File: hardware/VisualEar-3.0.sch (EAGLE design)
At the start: 8 parts

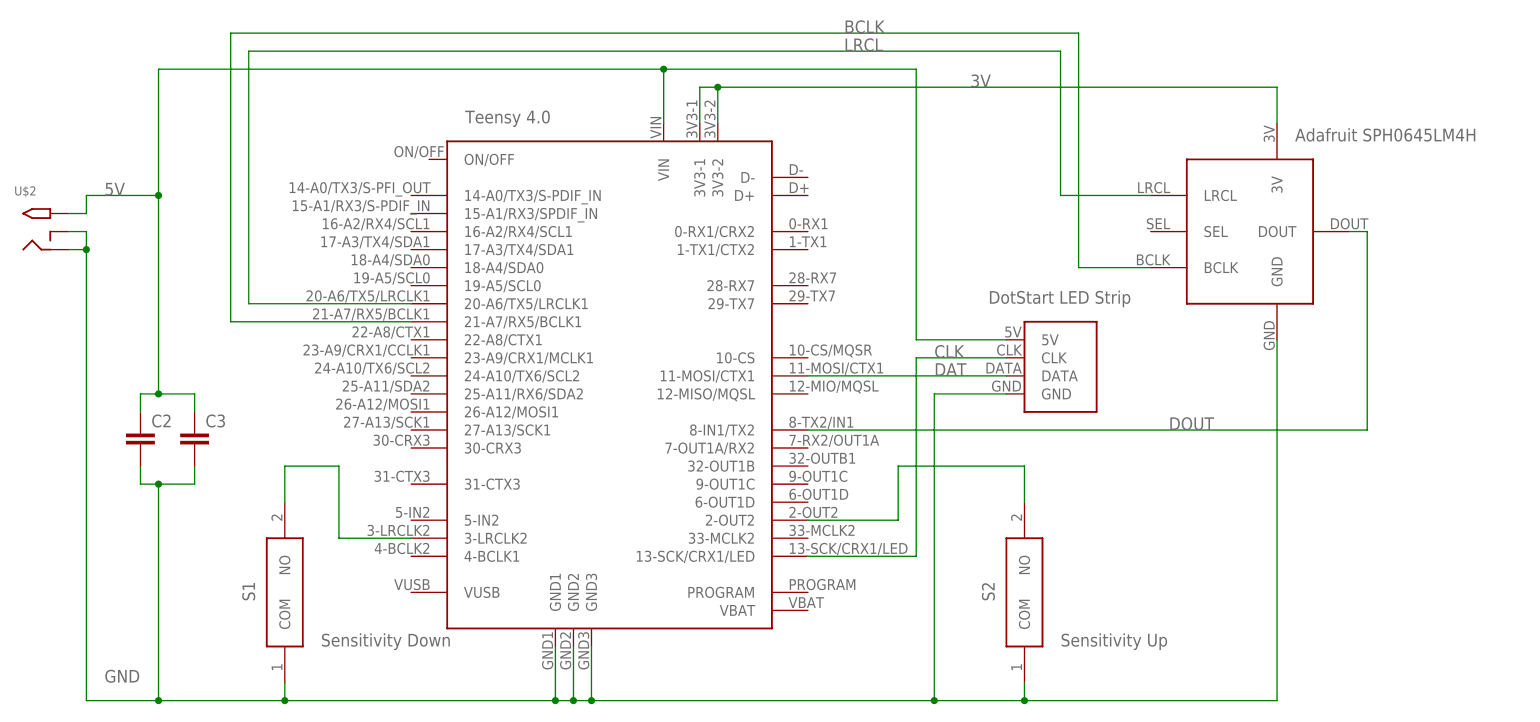
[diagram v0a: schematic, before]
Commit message: Updated to Single Button 3.0 PCB
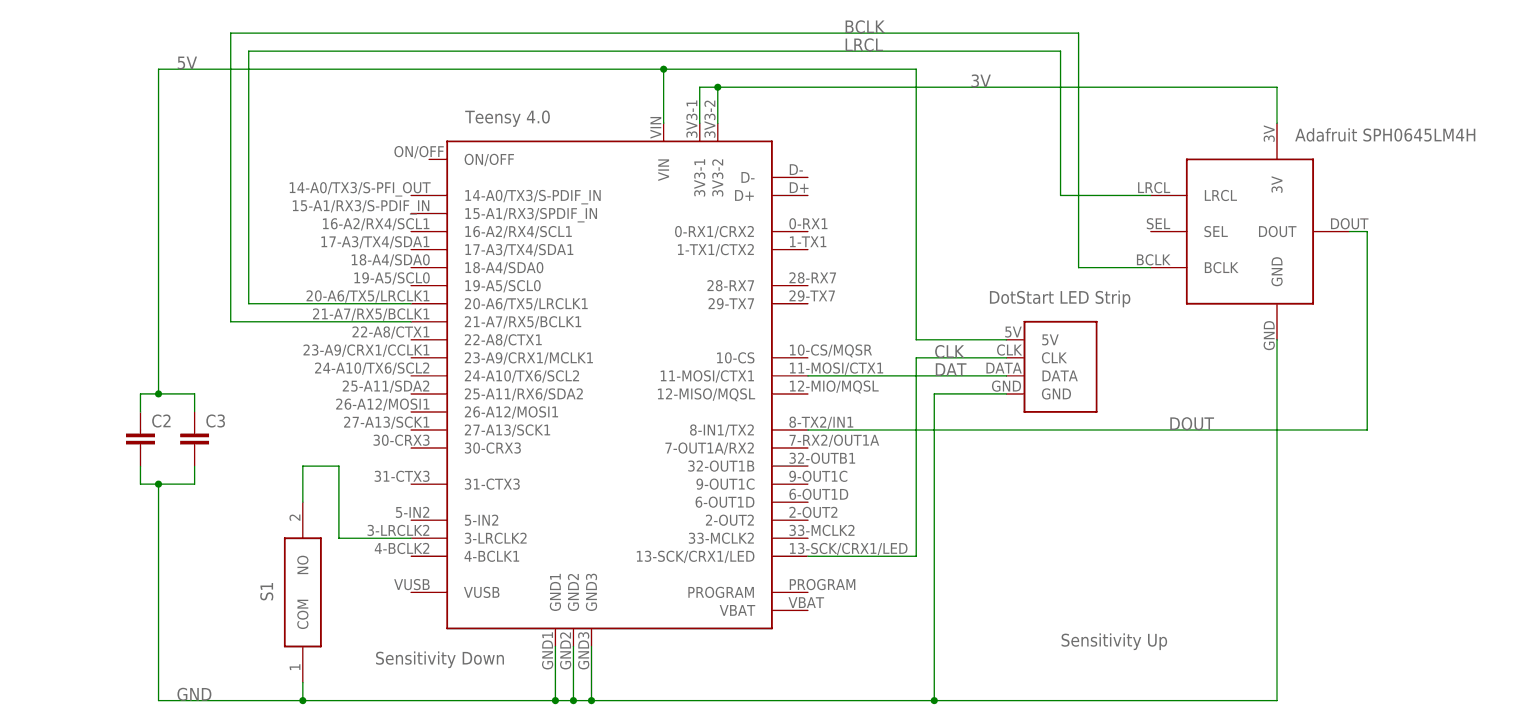
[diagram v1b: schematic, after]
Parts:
- removed S2: TACTILE-SWITCHTHRU-HOLE, philbot:TACTILE-SWITCHTHRU-HOLE
- removed U$2: 2.1MMJACKTHM, philbot:2.1MMJACKTHM
- C2, C3: device philbot:CAPPTH -> philbot:CAPPTH3
- U$1: value TEENSY40DIP -> TEENSY40DIPPLUS5; device teensy:TEENSY40DIP -> teensy:TEENSY40DIPPLUS5
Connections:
- removed net N$1: S2.NO, U$1.2-OUT2
- net 5V: no longer U$2.TIP
- net GND: no longer S2.COM, U$2.RING, U$2.RING_SW
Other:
- moved on the sheet: S1
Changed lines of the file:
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@@
 </classes>
 <parts>
-<part name="U$1" library="teensy" deviceset="TEENSY40" device="DIP" value="TEENSY40DIP"/>
-<part name="U$2" library="philbot" deviceset="2.1MMJACK" device="THM"/>
+<part name="U$1" library="teensy" deviceset="TEENSY40" device="DIPPLUS5" value="TEENSY40DIPPLUS5"/>
 <part name="U$3" library="philbot" deviceset="AF-I2S-MIC" device=""/>
 <part name="U$4" library="philbot" deviceset="LED-STRIP" device=""/>
-<part name="C2" library="philbot" deviceset="CAP" device="PTH"/>
-<part name="C3" library="philbot" deviceset="CAP" device="PTH"/>
+<part name="C2" library="philbot" deviceset="CAP" device="PTH3"/>
+<part name="C3" library="philbot" deviceset="CAP" device="PTH3"/>
 <part name="S1" library="philbot" deviceset="TACTILE-SWITCH" device="THRU-HOLE"/>
-<part name="S2" library="philbot" deviceset="TACTILE-SWITCH" device="THRU-HOLE"/>
 </parts>
 <sheets>
@@
 <text x="134.62" y="86.36" size="1.778" layer="95">Adafruit SPH0645LM4H</text>
 <text x="17.78" y="88.9" size="1.778" layer="95">Teensy 4.0</text>
-<text x="-2.54" y="15.24" size="1.778" layer="95">Sensitivity Down</text>
+<text x="5.08" y="12.7" size="1.778" layer="95">Sensitivity Down</text>
 <text x="101.6" y="15.24" size="1.778" layer="95">Sensitivity Up</text>
 </plain>
 <instances>
 <instance part="U$1" gate="G$1" x="38.1" y="55.88" smashed="yes"/>
-<instance part="U$2" gate="G$1" x="-43.18" y="73.66" smashed="yes">
-<attribute name="NAME" x="-45.72" y="78.74" size="1.27" layer="95"/>
-</instance>
 <instance part="U$3" gate="G$1" x="127" y="73.66" smashed="yes"/>
 <instance part="U$4" gate="G$1" x="99.06" y="53.34" smashed="yes"/>
@@
 <attribute name="VALUE" x="-18.796" y="41.021" size="1.778" layer="96"/>
 </instance>
-<instance part="S1" gate="G$1" x="-7.62" y="10.16" smashed="yes" rot="R90">
-<attribute name="NAME" x="-12.7" y="21.59" size="1.778" layer="95" rot="R90" align="center-left"/>
-</instance>
-<instance part="S2" gate="G$1" x="96.52" y="10.16" smashed="yes" rot="R90">
-<attribute name="NAME" x="91.44" y="21.59" size="1.778" layer="95" rot="R90" align="center-left"/>
+<instance part="S1" gate="G$1" x="-5.08" y="10.16" smashed="yes" rot="R90">
+<attribute name="NAME" x="-10.16" y="21.59" size="1.778" layer="95" rot="R90" align="center-left"/>
 </instance>
 </instances>
@@
 <net name="5V" class="0">
 <segment>
-<pinref part="U$2" gate="G$1" pin="TIP"/>
-<wire x1="-38.1" y1="76.2" x2="-35.56" y2="76.2" width="0.1524" layer="91"/>
-<wire x1="-35.56" y1="76.2" x2="-35.56" y2="78.74" width="0.1524" layer="91"/>
-<wire x1="-35.56" y1="78.74" x2="-25.4" y2="78.74" width="0.1524" layer="91"/>
 <pinref part="U$1" gate="G$1" pin="VIN"/>
 <wire x1="45.72" y1="88.9" x2="45.72" y2="96.52" width="0.1524" layer="91"/>
 <wire x1="45.72" y1="96.52" x2="-25.4" y2="96.52" width="0.1524" layer="91"/>
-<wire x1="-25.4" y1="96.52" x2="-25.4" y2="78.74" width="0.1524" layer="91"/>
 <junction x="45.72" y="96.52"/>
 <wire x1="45.72" y1="96.52" x2="81.28" y2="96.52" width="0.1524" layer="91"/>
@@
 <wire x1="-25.4" y1="50.8" x2="-20.32" y2="50.8" width="0.1524" layer="91"/>
 <wire x1="-20.32" y1="50.8" x2="-20.32" y2="48.26" width="0.1524" layer="91"/>
-<wire x1="-25.4" y1="78.74" x2="-25.4" y2="50.8" width="0.1524" layer="91"/>
-<junction x="-25.4" y="78.74"/>
+<wire x1="-25.4" y1="96.52" x2="-25.4" y2="50.8" width="0.1524" layer="91"/>
 <junction x="-25.4" y="50.8"/>
-<label x="-33.02" y="78.74" size="1.778" layer="95"/>
+<label x="-22.86" y="96.52" size="1.778" layer="95"/>
 </segment>
 </net>
@@
 <wire x1="35.56" y1="15.24" x2="35.56" y2="7.62" width="0.1524" layer="91"/>
 <wire x1="35.56" y1="7.62" x2="33.02" y2="7.62" width="0.1524" layer="91"/>
-<pinref part="U$2" gate="G$1" pin="RING"/>
 <wire x1="33.02" y1="7.62" x2="30.48" y2="7.62" width="0.1524" layer="91"/>
-<wire x1="30.48" y1="7.62" x2="-7.62" y2="7.62" width="0.1524" layer="91"/>
-<wire x1="-7.62" y1="7.62" x2="-25.4" y2="7.62" width="0.1524" layer="91"/>
-<wire x1="-25.4" y1="7.62" x2="-35.56" y2="7.62" width="0.1524" layer="91"/>
-<wire x1="-35.56" y1="7.62" x2="-35.56" y2="71.12" width="0.1524" layer="91"/>
-<wire x1="-35.56" y1="71.12" x2="-38.1" y2="71.12" width="0.1524" layer="91"/>
-<pinref part="U$2" gate="G$1" pin="RING_SW"/>
-<wire x1="-38.1" y1="73.66" x2="-35.56" y2="73.66" width="0.1524" layer="91"/>
-<wire x1="-35.56" y1="73.66" x2="-35.56" y2="71.12" width="0.1524" layer="91"/>
-<junction x="-35.56" y="71.12"/>
+<wire x1="30.48" y1="7.62" x2="-5.08" y2="7.62" width="0.1524" layer="91"/>
+<wire x1="-5.08" y1="7.62" x2="-25.4" y2="7.62" width="0.1524" layer="91"/>
 <pinref part="U$1" gate="G$1" pin="GND1"/>
 <wire x1="30.48" y1="15.24" x2="30.48" y2="7.62" width="0.1524" layer="91"/>
@@
 <pinref part="U$3" gate="G$1" pin="GND"/>
 <wire x1="35.56" y1="7.62" x2="83.82" y2="7.62" width="0.1524" layer="91"/>
-<wire x1="83.82" y1="7.62" x2="96.52" y2="7.62" width="0.1524" layer="91"/>
-<wire x1="96.52" y1="7.62" x2="132.08" y2="7.62" width="0.1524" layer="91"/>
+<wire x1="83.82" y1="7.62" x2="132.08" y2="7.62" width="0.1524" layer="91"/>
 <wire x1="132.08" y1="7.62" x2="132.08" y2="58.42" width="0.1524" layer="91"/>
 <junction x="35.56" y="7.62"/>
@@
 <wire x1="-25.4" y1="38.1" x2="-25.4" y2="7.62" width="0.1524" layer="91"/>
 <junction x="-25.4" y="38.1"/>
-<junction x="-25.4" y="7.62"/>
-<label x="-33.02" y="10.16" size="1.778" layer="95"/>
+<label x="-22.86" y="7.62" size="1.778" layer="95"/>
 <pinref part="S1" gate="G$1" pin="COM"/>
-<wire x1="-7.62" y1="10.16" x2="-7.62" y2="7.62" width="0.1524" layer="91"/>
-<junction x="-7.62" y="7.62"/>
-<pinref part="S2" gate="G$1" pin="COM"/>
-<wire x1="96.52" y1="10.16" x2="96.52" y2="7.62" width="0.1524" layer="91"/>
-<junction x="96.52" y="7.62"/>
-</segment>
-</net>
-<net name="N$1" class="0">
-<segment>
-<pinref part="U$1" gate="G$1" pin="2-OUT2"/>
-<wire x1="66.04" y1="33.02" x2="78.74" y2="33.02" width="0.1524" layer="91"/>
-<wire x1="78.74" y1="33.02" x2="78.74" y2="40.64" width="0.1524" layer="91"/>
-<wire x1="78.74" y1="40.64" x2="96.52" y2="40.64" width="0.1524" layer="91"/>
-<pinref part="S2" gate="G$1" pin="NO"/>
-<wire x1="96.52" y1="40.64" x2="96.52" y2="35.56" width="0.1524" layer="91"/>
+<wire x1="-5.08" y1="10.16" x2="-5.08" y2="7.62" width="0.1524" layer="91"/>
+<junction x="-5.08" y="7.62"/>
 </segment>
 </net>
@@
 <wire x1="0" y1="30.48" x2="0" y2="40.64" width="0.1524" layer="91"/>
 <pinref part="S1" gate="G$1" pin="NO"/>
-<wire x1="0" y1="40.64" x2="-7.62" y2="40.64" width="0.1524" layer="91"/>
-<wire x1="-7.62" y1="40.64" x2="-7.62" y2="35.56" width="0.1524" layer="91"/>
+<wire x1="0" y1="40.64" x2="-5.08" y2="40.64" width="0.1524" layer="91"/>
+<wire x1="-5.08" y1="40.64" x2="-5.08" y2="35.56" width="0.1524" layer="91"/>
 </segment>
 </net>
